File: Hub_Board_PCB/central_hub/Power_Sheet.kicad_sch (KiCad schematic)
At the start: 17 parts, among them J2 Barrel_Jack_MountingPin, U5 AP2112K-3.3TRG1, U6 AP63205WU-7

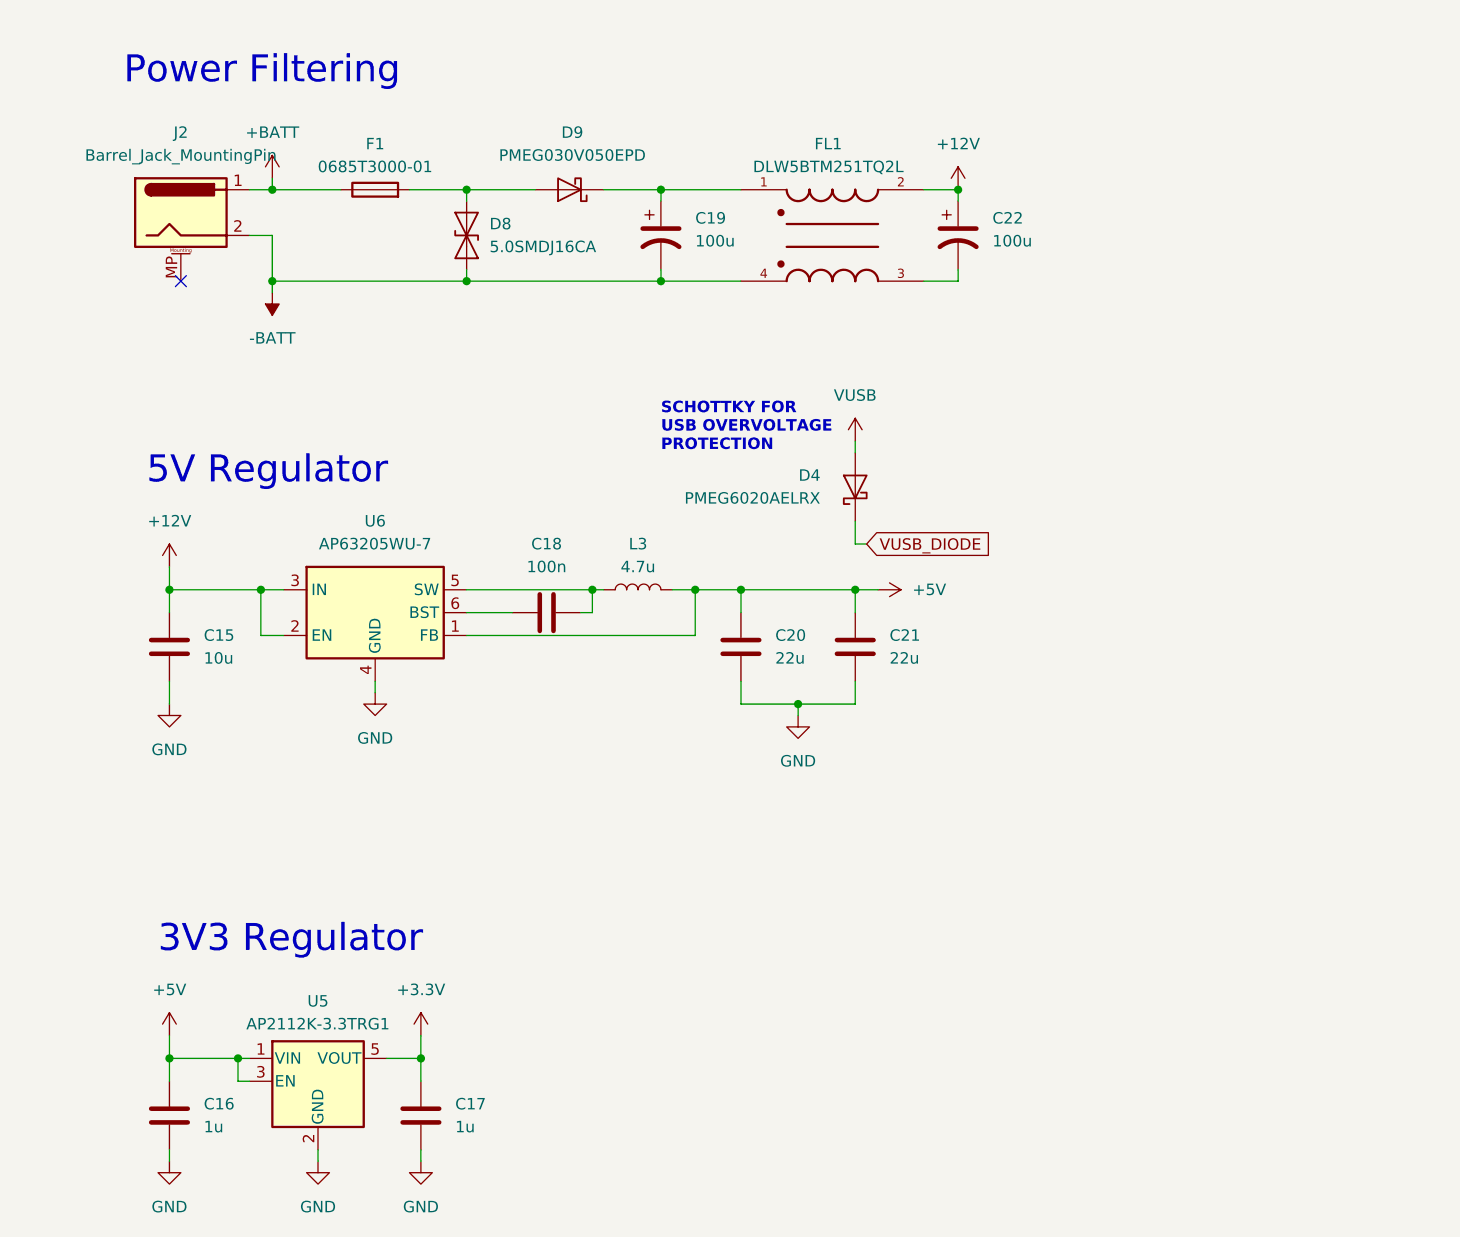
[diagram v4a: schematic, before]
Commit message: All library changes + hub power changes
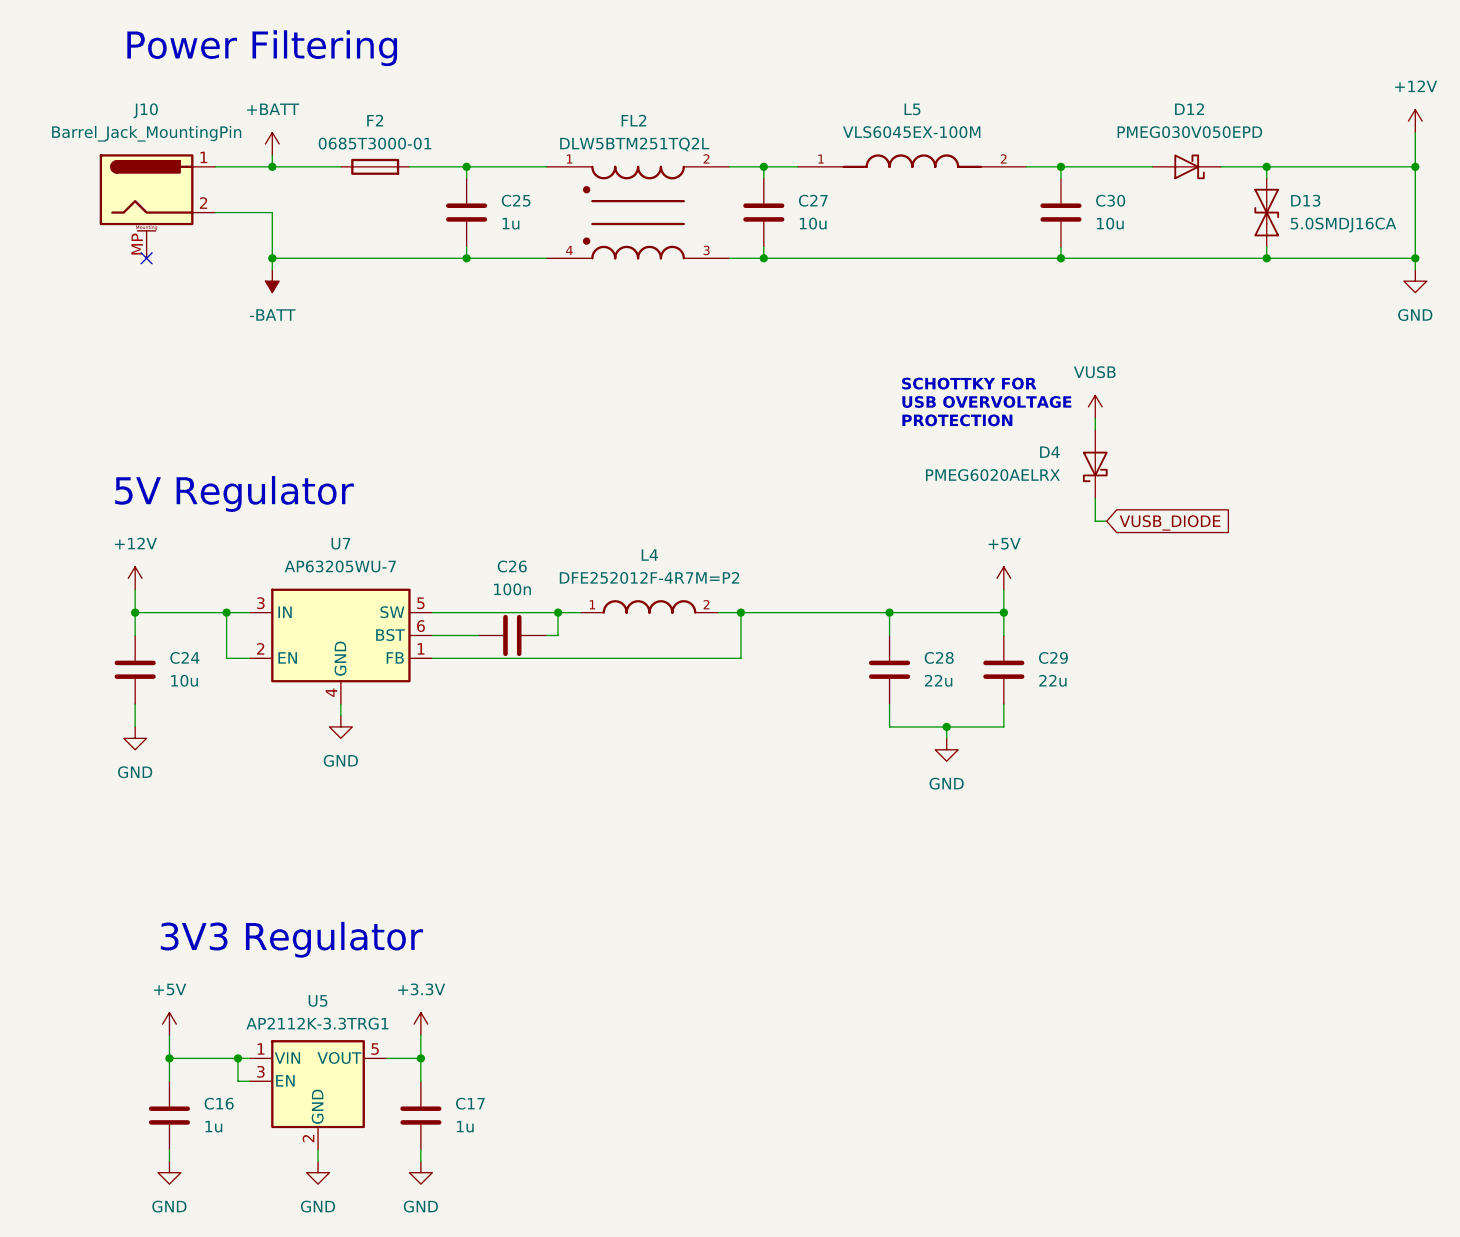
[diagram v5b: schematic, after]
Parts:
- removed C15: 10u, Capacitor_SMD:C_0603_1608Metric, symbol Device:C
- removed C18: 100n, Capacitor_SMD:C_0603_1608Metric, symbol Device:C
- removed C19, C22: 100u, Capacitor_SMD:C_0603_1608Metric, symbol Device:C_Polarized_US
- removed C20, C21: 22u, Capacitor_SMD:C_0603_1608Metric, symbol Device:C
- removed D8: 5.0SMDJ16CA, Diode_SMD:D_0603_1608Metric, symbol Diode:SMAJ18CA
- removed D9: PMEG030V050EPD, Package_TO_SOT_SMD:Nexperia_CFP15_SOT-1289, symbol Diode:PMEG030V050EPD
- removed F1: 0685T3000-01, Fuse:Fuse_0603_1608Metric, symbol Device:Fuse
- removed FL1: DLW5BTM251TQ2L, ~ALL:FIL_DLW5BTZ251TQ2L, symbol DLW5BTM251TQ2L:DLW5BTM251TQ2L
- removed J2: Barrel_Jack_MountingPin, Connector_BarrelJack:BarrelJack_CUI_PJ-063AH_Horizontal, symbol Connector:Barrel_Jack_MountingPin
- removed L3: 4.7u, ~ALL:IND_VLS6045EX-100M, symbol Device:L
- removed U6: AP63205WU-7, Package_TO_SOT_SMD:TSOT-23-6, symbol Regulator_Switching:AP63205WU
- added C24: 10u, Capacitor_SMD:C_0603_1608Metric, symbol Device:C
- added C25: 1u, Capacitor_SMD:C_1206_3216Metric, symbol Device:C
- added C26: 100n, Capacitor_SMD:C_0603_1608Metric, symbol Device:C
- added C27, C30: 10u, Capacitor_SMD:C_1210_3225Metric, symbol Device:C
- added C28, C29: 22u, Capacitor_SMD:C_0603_1608Metric, symbol Device:C
- added D12: PMEG030V050EPD, Package_TO_SOT_SMD:Nexperia_CFP15_SOT-1289, symbol Diode:PMEG030V050EPD
- added D13: 5.0SMDJ16CA, Diode_SMD:D_0603_1608Metric, symbol Diode:SMAJ18CA
- added F2: 0685T3000-01, Fuse:Fuse_1206_3216Metric, symbol Device:Fuse
- added FL2: DLW5BTM251TQ2L, ~ALL:FIL_DLW5BTZ251TQ2L, symbol DLW5BTM251TQ2L:DLW5BTM251TQ2L
- added J10: Barrel_Jack_MountingPin, Connector_BarrelJack:BarrelJack_CUI_PJ-063AH_Horizontal, symbol Connector:Barrel_Jack_MountingPin
- added L4: DFE252012F-4R7M=P2, ~ALL:INDC2520X120N, symbol DFE252012F-4R7M_P2:DFE252012F-4R7M=P2
- added L5: VLS6045EX-100M, ~ALL:IND_VLS6045EX-100M, symbol VLS6045EX-100M:VLS6045EX-100M
- added U7: AP63205WU-7, Package_TO_SOT_SMD:TSOT-23-6, symbol Regulator_Switching:AP63205WU
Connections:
- net GND is gone; now on net +12V: C16.1, C17.1, U5.2 (GND)
- net +12V: now also C24.1, C24.2, C27.1, C28.1, C29.1, C30.1, D12.3 (K), D13.1 (A1), D13.2 (A2), FL2.3, U7.2 (EN), U7.3 (IN), U7.4 (GND)
- net +5V: now also C28.2, C29.2, L4.2, U7.1 (FB)
- net +BATT: now also F2.1, J10.1
- net -BATT: now also C25.1, FL2.4, J10.2
- new net: C27.2, FL2.2, L5.1
- new net: C30.2, D12.1 (A), D12.2 (A), L5.2
- new net: C25.2, F2.2, FL2.1
- new net: C26.2, L4.1, U7.5 (SW)
- new net: C26.1, U7.6 (BST)
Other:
- moved on the sheet: D4

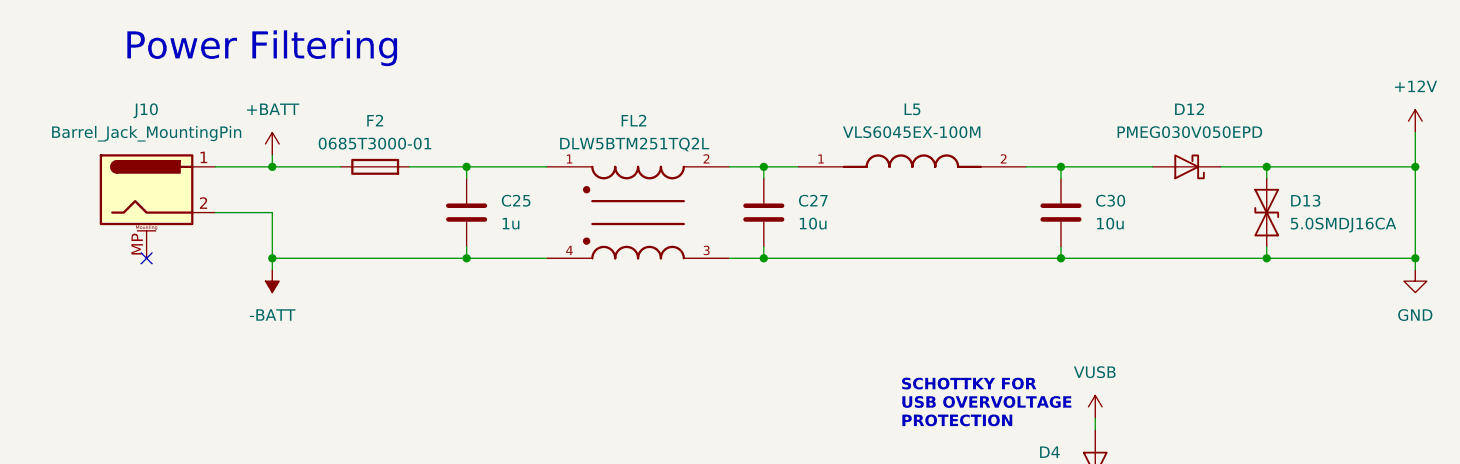
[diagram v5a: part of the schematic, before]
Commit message: Added cap on accel chip and switched power connector
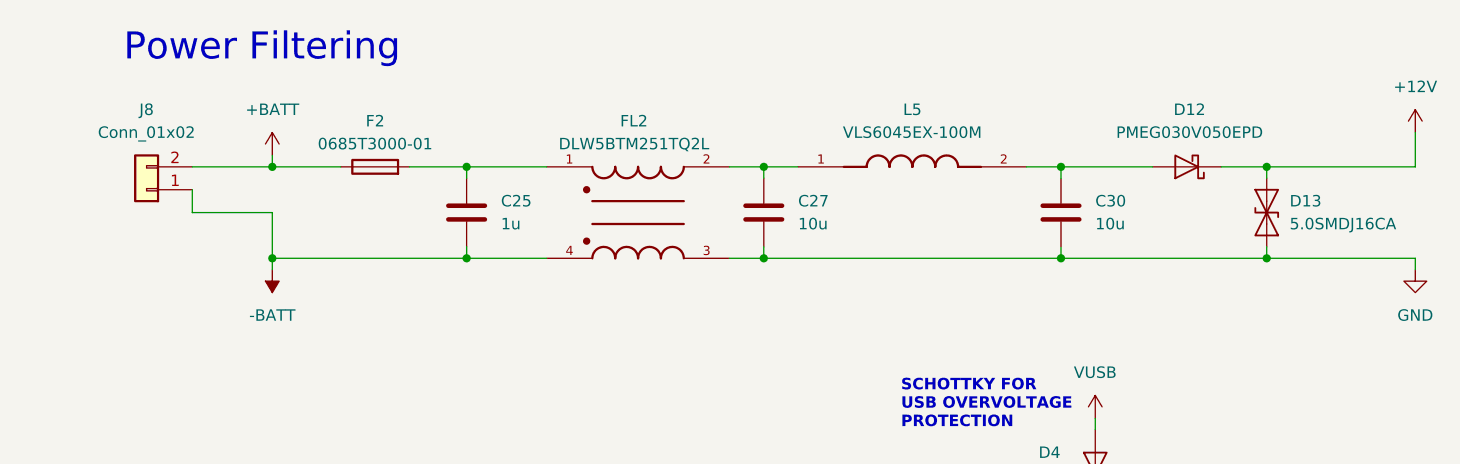
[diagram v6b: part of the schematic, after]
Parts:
- removed J10: Barrel_Jack_MountingPin, Connector_BarrelJack:BarrelJack_CUI_PJ-063AH_Horizontal, symbol Connector:Barrel_Jack_MountingPin
- added J8: Conn_01x02, Connector_PinHeader_2.54mm:PinHeader_1x02_P2.54mm_Vertical, symbol Connector_Generic:Conn_01x02
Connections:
- net +12V: no longer C16.1, C17.1, C24.1, C27.1, C28.1, C29.1, C30.1, D13.1 (A1), FL2.3, U5.2 (GND), U7.4 (GND)
- net +BATT: now also J8.2 (Pin_2)
- net -BATT: now also J8.1 (Pin_1)
- new net GND: C16.1, C17.1, C24.1, C27.1, C28.1, C29.1, C30.1, D13.1 (A1), FL2.3, U5.2 (GND), U7.4 (GND)
- no-connect marks 1 -> 0
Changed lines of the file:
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@@
   (junction (at 40.64 144.78) (diameter 0) (color 0 0 0 0)
   )
-  (junction (at 179.07 45.72) (diameter 0) (color 0 0 0 0)
-  )
   (junction (at 162.56 55.88) (diameter 0) (color 0 0 0 0)
   )
@@
   (junction (at 52.07 55.88) (diameter 0) (color 0 0 0 0)
   )
-  (junction (at 179.07 55.88) (diameter 0) (color 0 0 0 0)
-  )
   (junction (at 106.68 55.88) (diameter 0) (color 0 0 0 0)
   )
@@
   (junction (at 106.68 45.72) (diameter 0) (color 0 0 0 0)
   )
-  (no_connect (at 38.1 55.88))
-  (wire (pts (xy 45.72 50.8) (xy 52.07 50.8))
+  (wire (pts (xy 43.18 50.8) (xy 52.07 50.8))
     (stroke (width 0) (type default))
   )
@@
     (stroke (width 0) (type default))
   )
-  (wire (pts (xy 179.07 45.72) (xy 179.07 55.88))
-    (stroke (width 0) (type default))
-  )
   (wire (pts (xy 127 107.95) (xy 127 109.22))
     (stroke (width 0) (type default))
@@
     (stroke (width 0) (type default))
   )
-  (wire (pts (xy 45.72 45.72) (xy 52.07 45.72))
+  (wire (pts (xy 43.18 45.72) (xy 52.07 45.72))
     (stroke (width 0) (type default))
   )
@@
   )
   (wire (pts (xy 36.83 105.41) (xy 36.83 107.95))
+    (stroke (width 0) (type default))
+  )
+  (wire (pts (xy 43.18 50.8) (xy 43.18 48.26))
     (stroke (width 0) (type default))
   )
@@
     )
   )
+  (symbol (lib_id "Connector_Generic:Conn_01x02") (at 38.1 48.26 180) (unit 1)
+    (in_bom yes) (on_board yes) (dnp no) (fields_autoplaced)
+    (property "Reference" "J8" (at 38.1 39.37 0)
+      (effects (font (size 1.27 1.27)))
+    )
+    (property "Value" "Conn_01x02" (at 38.1 41.91 0)
+      (effects (font (size 1.27 1.27)))
+    )
+    (property "Footprint" "Connector_PinHeader_2.54mm:PinHeader_1x02_P2.54mm_Vertical" (at 38.1 48.26 0)
+      (effects (font (size 1.27 1.27)) hide)
+    )
+    (property "Datasheet" "~" (at 38.1 48.26 0)
+      (effects (font (size 1.27 1.27)) hide)
+    )
+    (pin "1")
+    (pin "2")
+    (instances
+      (project "central_hub"
+        (path "/0d9ec66e-0fbf-4d12-9b83-adf78971a00b/8e53aed1-21e6-440d-aae4-1b5509ec346a"
+          (reference "J8") (unit 1)
+        )
+        (path "/0d9ec66e-0fbf-4d12-9b83-adf78971a00b/5d965db6-20f7-4bcf-a9c5-180dec6abb05"
+          (reference "J2") (unit 1)
+        )
+      )
+      (project "motor_board_pcb"
+        (path "/4ad82a24-c992-45c9-b523-12e12bcd6ced/996060af-581e-425f-9e10-26ee39d5a960"
+          (reference "J8") (unit 1)
+        )
+      )
+    )
+  )
   (symbol (lib_id "VLS6045EX-100M:VLS6045EX-100M") (at 123.19 45.72 0) (unit 1)
     (in_bom yes) (on_board yes) (dnp no) (fields_autoplaced)
@@
         )
       )
-    )
-  )
-  (symbol (lib_id "Connector:Barrel_Jack_MountingPin") (at 38.1 48.26 0) (unit 1)
-    (in_bom yes) (on_board yes) (dnp no) (fields_autoplaced)
-    (property "Reference" "J10" (at 38.1 39.37 0)
-      (effects (font (size 1.27 1.27)))
-    )
-    (property "Value" "Barrel_Jack_MountingPin" (at 38.1 41.91 0)
-      (effects (font (size 1.27 1.27)))
-    )
-    (property "Footprint" "Connector_BarrelJack:BarrelJack_CUI_PJ-063AH_Horizontal" (at 39.37 49.276 0)
-      (effects (font (size 1.27 1.27)) hide)
-    )
-    (property "Datasheet" "~" (at 39.37 49.276 0)
-      (effects (font (size 1.27 1.27)) hide)
-    )
-    (pin "1")
-    (pin "2")
-    (pin "MP")
-    (instances
-      (project "central_hub"
-        (path "/0d9ec66e-0fbf-4d12-9b83-adf78971a00b/5d965db6-20f7-4bcf-a9c5-180dec6abb05"
-          (reference "J10") (unit 1)
-        )
-      )
-      (project "motor_board_pcb"
-        (path "/4ad82a24-c992-45c9-b523-12e12bcd6ced/8b03500d-82ba-403b-affc-552426d5b4ea"
-          (reference "J6") (unit 1)
-        )
-      )

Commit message: Schematic changes before sending to kim
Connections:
- net +BATT: now also J8.1 (Pin_1); no longer J8.2 (Pin_2)
- net -BATT: now also J8.2 (Pin_2); no longer J8.1 (Pin_1)
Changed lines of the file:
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@@
-    )
-  )
-  (symbol (lib_id "Connector_Generic:Conn_01x02") (at 38.1 48.26 180) (unit 1)
-    (in_bom yes) (on_board yes) (dnp no) (fields_autoplaced)
-    (property "Reference" "J8" (at 38.1 39.37 0)
-      (effects (font (size 1.27 1.27)))
-    )
-    (property "Value" "Conn_01x02" (at 38.1 41.91 0)
-      (effects (font (size 1.27 1.27)))
-    )
-    (property "Footprint" "Connector_PinHeader_2.54mm:PinHeader_1x02_P2.54mm_Vertical" (at 38.1 48.26 0)
-      (effects (font (size 1.27 1.27)) hide)
-    )
-    (property "Datasheet" "~" (at 38.1 48.26 0)
-      (effects (font (size 1.27 1.27)) hide)
-    )
-    (pin "1")
-    (pin "2")
-    (instances
-      (project "central_hub"
-        (path "/0d9ec66e-0fbf-4d12-9b83-adf78971a00b/8e53aed1-21e6-440d-aae4-1b5509ec346a"
-          (reference "J8") (unit 1)
-        )
-        (path "/0d9ec66e-0fbf-4d12-9b83-adf78971a00b/5d965db6-20f7-4bcf-a9c5-180dec6abb05"
-          (reference "J2") (unit 1)
-        )
-      )
-      (project "motor_board_pcb"
-        (path "/4ad82a24-c992-45c9-b523-12e12bcd6ced/996060af-581e-425f-9e10-26ee39d5a960"
-          (reference "J8") (unit 1)
-        )
-      )
     )
   )
@@
         )
       )
+    )
+  )
+  (symbol (lib_id "Connector_Generic:Conn_01x02") (at 38.1 45.72 0) (mirror y) (unit 1)
+    (in_bom yes) (on_board yes) (dnp no)
+    (property "Reference" "J8" (at 38.1 54.61 0)
+      (effects (font (size 1.27 1.27)))
+    )
+    (property "Value" "Conn_01x02" (at 38.1 52.07 0)
+      (effects (font (size 1.27 1.27)))
+    )
+    (property "Footprint" "Connector_PinHeader_2.54mm:PinHeader_1x02_P2.54mm_Vertical" (at 38.1 45.72 0)
+      (effects (font (size 1.27 1.27)) hide)
+    )
+    (property "Datasheet" "~" (at 38.1 45.72 0)
+      (effects (font (size 1.27 1.27)) hide)
+    )
+    (pin "1")
+    (pin "2")
+    (instances
+      (project "central_hub"
+        (path "/0d9ec66e-0fbf-4d12-9b83-adf78971a00b/8e53aed1-21e6-440d-aae4-1b5509ec346a"
+          (reference "J8") (unit 1)
+        )
+        (path "/0d9ec66e-0fbf-4d12-9b83-adf78971a00b/5d965db6-20f7-4bcf-a9c5-180dec6abb05"
+          (reference "J2") (unit 1)
+        )
+      )
+      (project "motor_board_pcb"
+        (path "/4ad82a24-c992-45c9-b523-12e12bcd6ced/996060af-581e-425f-9e10-26ee39d5a960"
+          (reference "J8") (unit 1)
+        )
+      )
